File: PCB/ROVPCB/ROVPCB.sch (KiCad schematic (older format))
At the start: 15 parts, among them J1 Conn_01x04_Male, J2 Conn_01x04_Male, P1 Conn_02x20_Odd_Even, U1 MPU-9250, U2 BME280, U3 LIGHT_TSL2591, U4 LTC4316IDDPBF

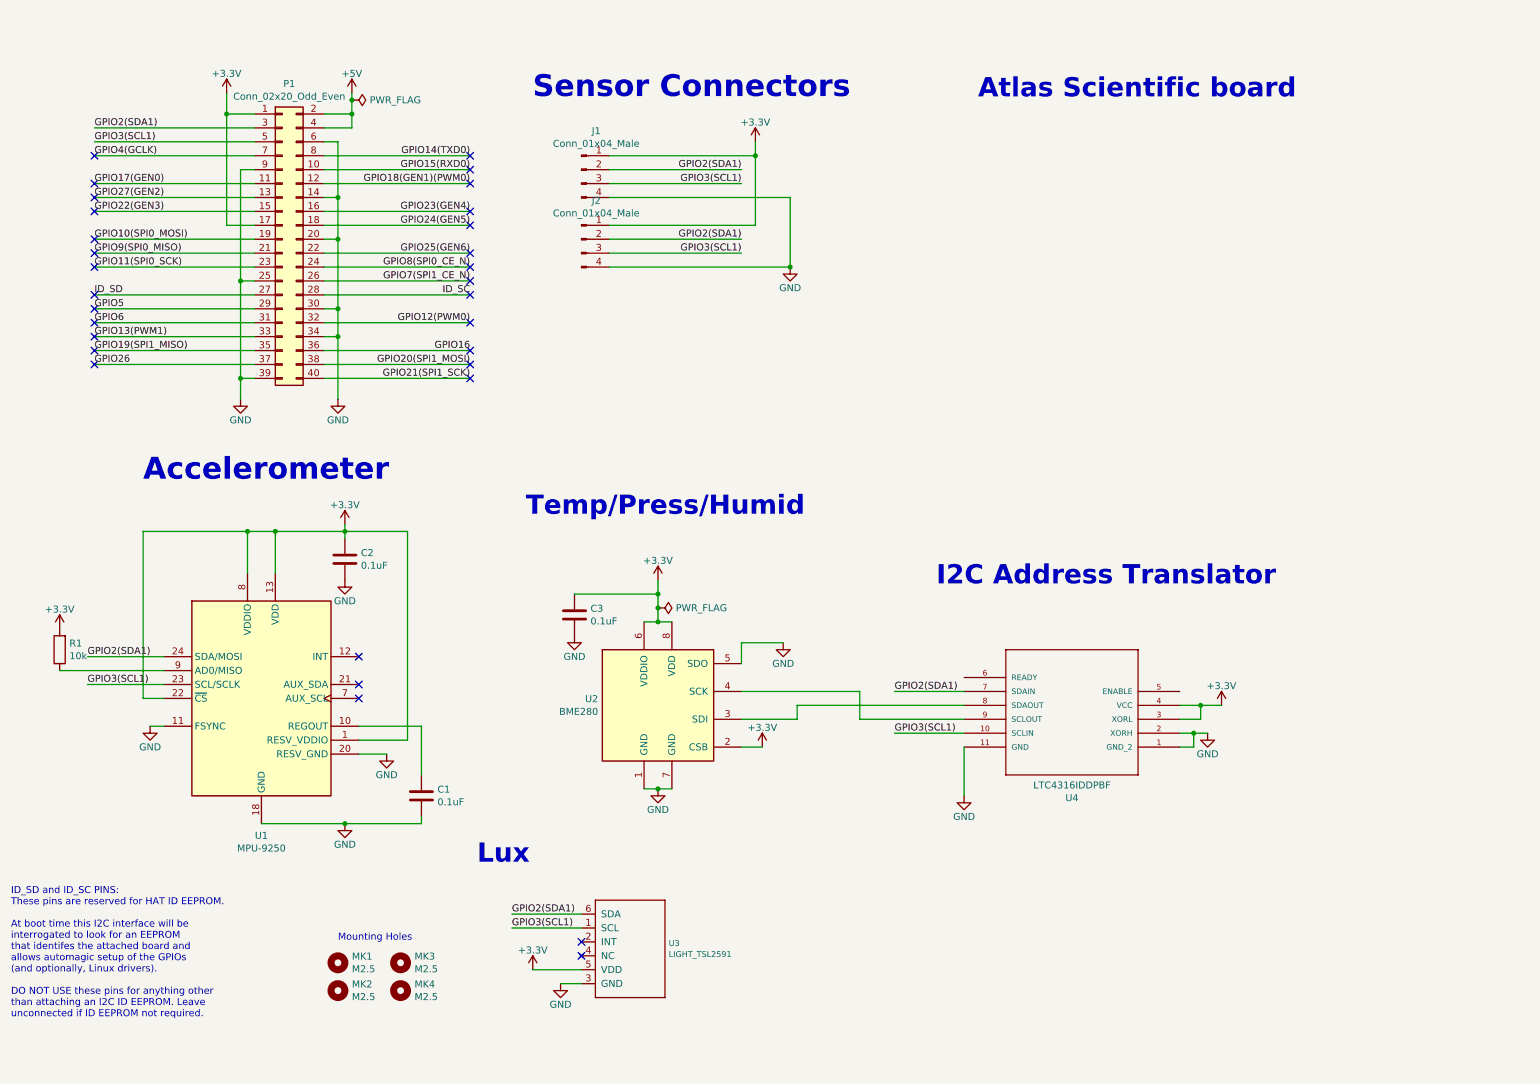
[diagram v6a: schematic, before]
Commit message: Added I2C addresses to schematic and other housekeeping stuff
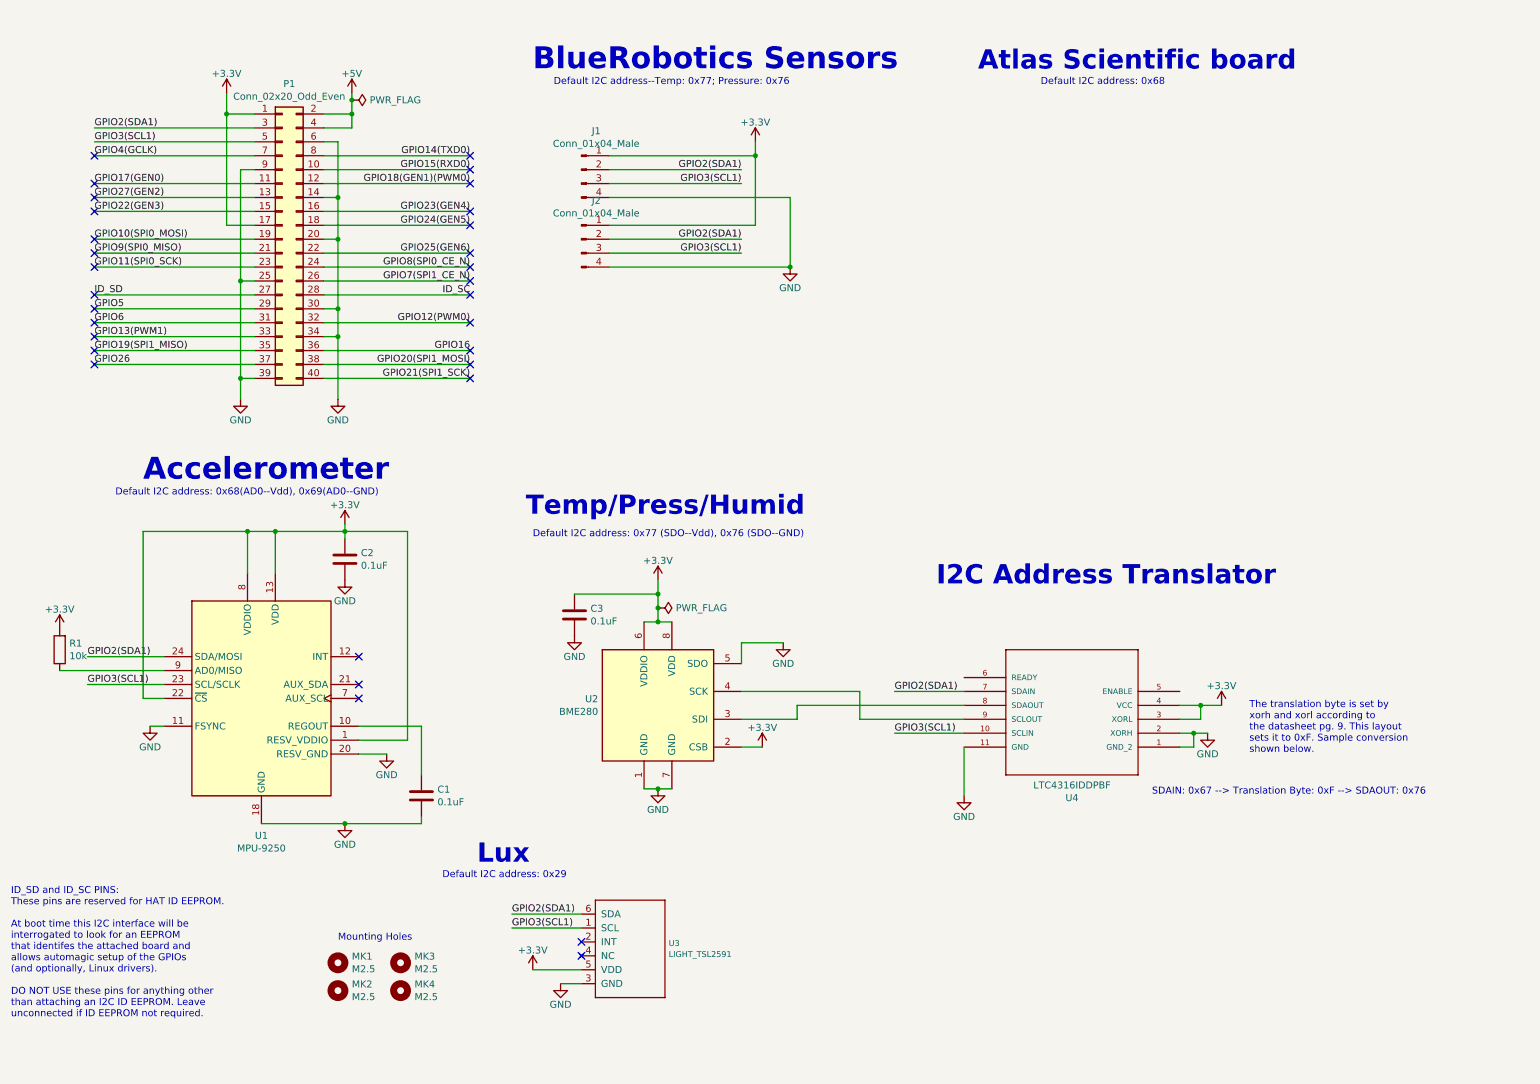
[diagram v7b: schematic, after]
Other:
- note added: "BlueRobotics Sensors"
- note added: "Default I2C address--Temp: 0x77; Pressure: 0x76"
- note added: "Default I2C address: 0x29"
- note added: "Default I2C address: 0x68"
- note added: "Default I2C address: 0x68(AD0--Vdd), 0x69(AD0--GND)"
- note added: "Default I2C address: 0x77 (SDO--Vdd), 0x76 (SDO--GND)"
- note added: "SDAIN: 0x67 --> Translation Byte: 0xF --> SDAOUT: 0x76"
- note added: "The translation byte is set by \nxorh and xorl according to \nthe datasheet pg. 9. This layout\nsets it to 0xF. Sample conversion\nshown below."
- note removed: "Sensor Connectors"
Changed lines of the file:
@@
 	1    0    0    -1
 $EndComp
-Text Notes 4400 1000 0    157  ~ 31
-Sensor Connectors
+Text Notes 4400 800  0    157  ~ 31
+BlueRobotics Sensors
 Text Label 5900 1500 2    50   ~ 0
 GPIO2(SDA1)
@@
 F 1 "BME280" H 4870 5305 50  0000 R CNN
 F 2 "Package_LGA:Bosch_LGA-8_2.5x2.5mm_P0.65mm_ClockwisePinNumbering" H 5300 5150 50  0001 C CNN
-F 3 "https://ae-bst.resource.bosch.com/media/_tech/media/datasheets/BST-BME280_DS001-11.pdf" H 5300 5150 50  0001 C CNN
+F 3 "https://cdn-shop.adafruit.com/datasheets/BST-BME280_DS001-10.pdf" H 5300 5150 50  0001 C CNN
 	1    5300 5350
 	1    0    0    -1
@@
 Wire Wire Line
 	5300 4550 5300 4650
-$Comp
-L ROVPCB-rescue:GND-power-ROVPCB-rescue-ROVPCB-rescue #PWR0111
-U 1 1 5CB97771
-P 6200 4900
-F 0 "#PWR0111" H 6200 4650 50  0001 C CNN
-F 1 "GND" H 6200 4750 50  0000 C CNN
-F 2 "" H 6200 4900 50  0000 C CNN
-F 3 "" H 6200 4900 50  0000 C CNN
-	1    6200 4900
-	1    0    0    -1
-$EndComp
 Wire Wire Line
 	6200 4900 5900 4900
@@
 F 1 "LTC4316IDDPBF" H 11525 5924 50  0000 C CNN
 F 2 "LTC4316IDDPBF:DFN-10_DD" H 13450 5150 50  0001 L BNN
-F 3 "LTC4316IDD#PBF-ND" H 13250 5650 50  0001 L BNN
+F 3 "https://www.analog.com/media/en/technical-documentation/data-sheets/4316fa.pdf" H 13250 5650 50  0001 L BNN
 F 4 "Linear Technology/Analog" H 13100 5950 50  0001 L BNN "Field4"
 F 5 "LTC4316 - Single I2C/SMBus Address Translator" H 12700 5800 50  0001 L BNN "Field5"
@@
 	-1   0    0    1
 $EndComp
-Text Notes 7600 1000 0    138  ~ 28
+Text Notes 7600 800  0    138  ~ 28
 Atlas Scientific board
 Text Label 7000 5250 0    50   ~ 0
@@
 Wire Wire Line
 	9150 5550 9050 5550
+Text Notes 8850 6000 0    50   ~ 0
+SDAIN: 0x67 --> Translation Byte: 0xF --> SDAOUT: 0x76
+Text Notes 9550 5700 0    50   ~ 0
+The translation byte is set by \nxorh and xorl according to \nthe datasheet pg. 9. This layout\nsets it to 0xF. Sample conversion\nshown below.
+Text Notes 4400 4150 0    50   ~ 0
+Default I2C address: 0x77 (SDO--Vdd), 0x76 (SDO--GND)
+Text Notes 1400 3850 0    50   ~ 0
+Default I2C address: 0x68(AD0--Vdd), 0x69(AD0--GND)
+Text Notes 3750 6600 0    50   ~ 0
+Default I2C address: 0x29
+Text Notes 8050 900  0    50   ~ 0
+Default I2C address: 0x68
+Text Notes 4550 900  0    50   ~ 0
+Default I2C address--Temp: 0x77; Pressure: 0x76
+$Comp
+L ROVPCB-rescue:GND-power-ROVPCB-rescue-ROVPCB-rescue #PWR?
+U 1 1 5CBDF2B2
+P 6200 4900
+F 0 "#PWR?" H 6200 4650 50  0001 C CNN
+F 1 "GND" H 6200 4750 50  0000 C CNN
+F 2 "" H 6200 4900 50  0000 C CNN
+F 3 "" H 6200 4900 50  0000 C CNN
+	1    6200 4900
+	1    0    0    -1
+$EndComp
 $EndSCHEMATC

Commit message: Adding the Atlas Board... BNC??
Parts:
- added U5: AtlasOEM, Adafruit TSL2591:OEM Board, symbol Adafruit_TSL2591-eagle-import:AtlasOEM
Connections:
- net +3V3: now also U5.3 (Vcc)
- net GND: now also U5.6 (GND)
- net GPIO2(SDA1): now also U5.1 (SDA)
- net GPIO3(SCL1): now also U5.8 (SCL)
- no-connect marks 31 -> 35
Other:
- note added: "Default I2C address: 0x64"
- note removed: "Default I2C address: 0x68"
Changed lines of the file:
@@
 	7000 5250 7500 5250
 $Comp
-L ROVPCB-rescue:GND-power-ROVPCB-rescue-ROVPCB-rescue #PWR?
+L ROVPCB-rescue:GND-power-ROVPCB-rescue-ROVPCB-rescue #PWR0111
 U 1 1 5CB8FA80
 P 7500 6000
-F 0 "#PWR?" H 7500 5750 50  0001 C CNN
+F 0 "#PWR0111" H 7500 5750 50  0001 C CNN
 F 1 "GND" H 7500 5850 50  0000 C CNN
 F 2 "" H 7500 6000 50  0000 C CNN
@@
 	6750 5450 7500 5450
 $Comp
-L ROVPCB-rescue:GND-power-ROVPCB-rescue-ROVPCB-rescue #PWR?
+L ROVPCB-rescue:GND-power-ROVPCB-rescue-ROVPCB-rescue #PWR0112
 U 1 1 5CBA3506
 P 9250 5550
-F 0 "#PWR?" H 9250 5300 50  0001 C CNN
+F 0 "#PWR0112" H 9250 5300 50  0001 C CNN
 F 1 "GND" H 9250 5400 50  0000 C CNN
 F 2 "" H 9250 5550 50  0000 C CNN
@@
 	9250 5550 9150 5550
 $Comp
-L ROVPCB-rescue:+3.3V-power-ROVPCB-rescue-ROVPCB-rescue #PWR?
+L ROVPCB-rescue:+3.3V-power-ROVPCB-rescue-ROVPCB-rescue #PWR0113
 U 1 1 5CBA6BEC
 P 9350 5350
-F 0 "#PWR?" H 9350 5200 50  0001 C CNN
+F 0 "#PWR0113" H 9350 5200 50  0001 C CNN
 F 1 "+3.3V" H 9350 5490 50  0000 C CNN
 F 2 "" H 9350 5350 50  0000 C CNN
@@
 Default I2C address: 0x29
 Text Notes 8050 900  0    50   ~ 0
-Default I2C address: 0x68
+Default I2C address: 0x64
 Text Notes 4550 900  0    50   ~ 0
 Default I2C address--Temp: 0x77; Pressure: 0x76
 $Comp
-L ROVPCB-rescue:GND-power-ROVPCB-rescue-ROVPCB-rescue #PWR?
+L ROVPCB-rescue:GND-power-ROVPCB-rescue-ROVPCB-rescue #PWR0114
 U 1 1 5CBDF2B2
 P 6200 4900
-F 0 "#PWR?" H 6200 4650 50  0001 C CNN
+F 0 "#PWR0114" H 6200 4650 50  0001 C CNN
 F 1 "GND" H 6200 4750 50  0000 C CNN
 F 2 "" H 6200 4900 50  0000 C CNN
@@
 	1    0    0    -1
 $EndComp
+$Comp
+L Adafruit_TSL2591-eagle-import:AtlasOEM U5
+U 1 1 5CBE687D
+P 8650 1400
+F 0 "U5" H 8650 1775 50  0000 C CNN
+F 1 "AtlasOEM" H 8650 1684 50  0000 C CNN
+F 2 "Adafruit TSL2591:OEM Board" H 8650 1400 50  0001 C CNN
+F 3 "https://www.atlas-scientific.com/_files/_datasheets/_oem/EC_oem_datasheet.pdf" H 8650 1400 50  0001 C CNN
+	1    8650 1400
+	1    0    0    -1
+$EndComp
+NoConn ~ 9000 1250
+NoConn ~ 9000 1350
+NoConn ~ 8300 1350
+Text Label 7800 1250 0    50   ~ 0
+GPIO2(SDA1)
+Wire Wire Line
+	7800 1250 8300 1250
+Text Label 9550 1450 2    50   ~ 0
+GPIO3(SCL1)
+Wire Wire Line
+	9550 1450 9000 1450
+$Comp
+L ROVPCB-rescue:GND-power-ROVPCB-rescue-ROVPCB-rescue #PWR?
+U 1 1 5CBFDF85
+P 9250 1650
+F 0 "#PWR?" H 9250 1400 50  0001 C CNN
+F 1 "GND" H 9250 1500 50  0000 C CNN
+F 2 "" H 9250 1650 50  0000 C CNN
+F 3 "" H 9250 1650 50  0000 C CNN
+	1    9250 1650
+	1    0    0    -1
+$EndComp
+Wire Wire Line
+	9250 1650 9000 1650
+$Comp
+L ROVPCB-rescue:+3.3V-power-ROVPCB-rescue-ROVPCB-rescue #PWR?
+U 1 1 5CC01F57
+P 7750 1450
+F 0 "#PWR?" H 7750 1300 50  0001 C CNN
+F 1 "+3.3V" H 7750 1590 50  0000 C CNN
+F 2 "" H 7750 1450 50  0000 C CNN
+F 3 "" H 7750 1450 50  0000 C CNN
+	1    7750 1450
+	1    0    0    -1
+$EndComp
+Wire Wire Line
+	7750 1450 8300 1450
+NoConn ~ 9000 1550
 $EndSCHEMATC
